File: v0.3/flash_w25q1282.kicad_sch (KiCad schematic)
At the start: 4 parts, among them IC5 W25Q128JVSIM_TR

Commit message: v0.3: lots of routing done
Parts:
- removed NT2: NetTie_2, symbol Device:NetTie_2
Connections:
- net FLASH_3V3 is gone; now on net +3.3V: C39.1, C40.1, IC5.8 (VCC)
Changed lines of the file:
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@@
-	(wire
-		(pts
-			(xy 228.6 105.41) (xy 242.57 105.41)
-		)
-		(stroke
-			(width 0)
-			(type default)
-		)
-	)
 	(wire
 		(pts
@@
 	(wire
 		(pts
-			(xy 212.09 105.41) (xy 223.52 105.41)
+			(xy 212.09 105.41) (xy 242.57 105.41)
 		)
 		(stroke
@@
 					(unit 1)
 				)
-			)
-		)
-	)
-	(symbol
-		(lib_id "Device:NetTie_2")
-		(at 226.06 105.41 0)
-		(unit 1)
-		(exclude_from_sim no)
-		(in_bom no)
-		(on_board yes)
-		(dnp no)
-		(fields_autoplaced yes)
-		(property "Reference" "NT2"
-			(at 226.06 100.33 0)
-			(effects
-				(font
-					(size 1.27 1.27)
-				)
-			)
-		)
-		(property "Value" "NetTie_2"
-			(at 226.06 102.87 0)
-			(effects
-				(font
-					(size 1.27 1.27)
-				)
-			)
-		)
-		(property "Footprint" ""
-			(at 226.06 105.41 0)
-			(effects
-				(font
-					(size 1.27 1.27)
-				)
-				(hide yes)
-			)
-		)
-		(property "Datasheet" "~"
-			(at 226.06 105.41 0)
-			(effects
-				(font
-					(size 1.27 1.27)
-				)
-				(hide yes)
-			)
-		)
-		(property "Description" "Net tie, 2 pins"
-			(at 226.06 105.41 0)
-			(effects
-				(font
-					(size 1.27 1.27)
-				)
-				(hide yes)
-			)
-		)
-		(pin "1"
-		)
-		(pin "2"
-		)
-		(instances
-			(project ""
-				(path "/5cbb45d4-7f83-48dd-a53b-5c75c7d1d827/d61d67cb-51a7-4693-85fc-ed7a034bf235"
-					(reference "NT2")
-					(unit 1)
-				)

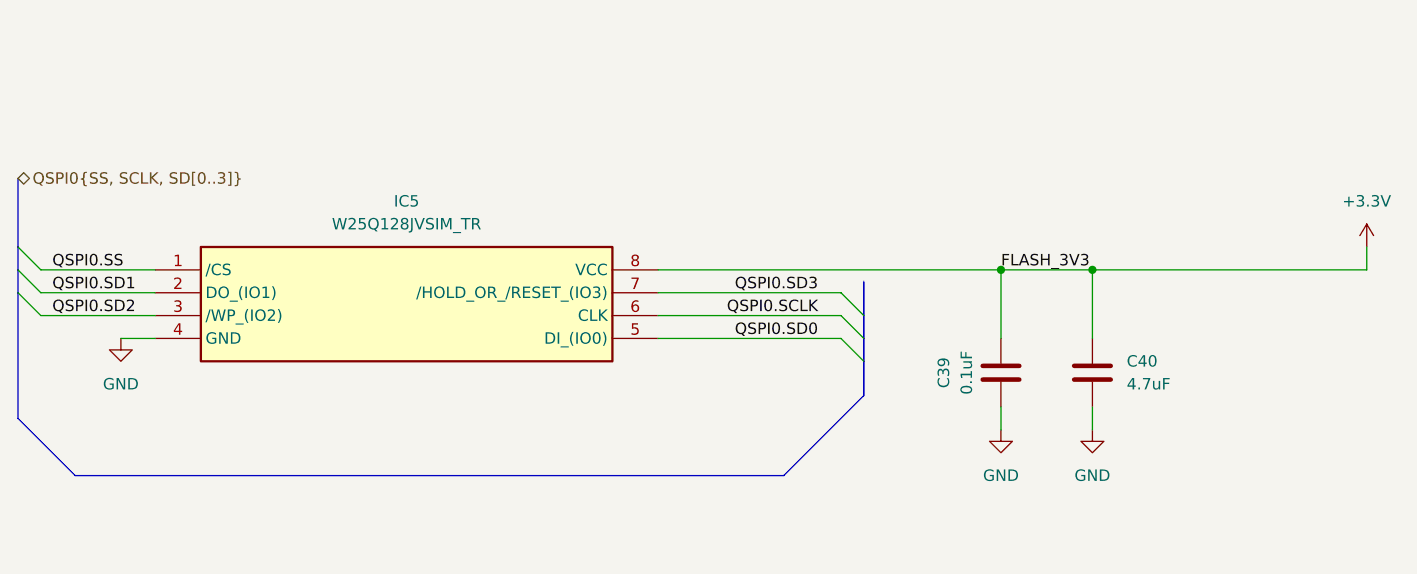
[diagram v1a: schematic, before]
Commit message: v0.3: move pmic to right side of board
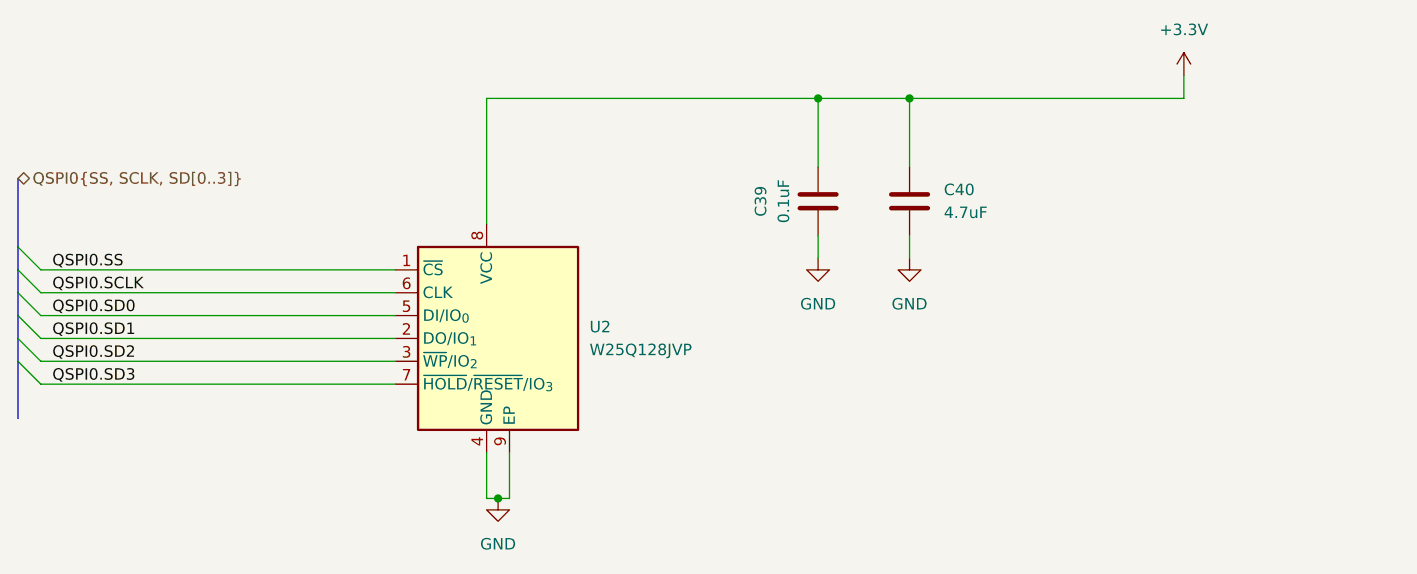
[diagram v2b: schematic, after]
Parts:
- removed IC5: W25Q128JVSIM_TR, SamacSys_Parts:SOIC127P790X216-8N, symbol SamacSys_Parts:W25Q128JVSIM_TR
- added U2: W25Q128JVP, Package_SON:WSON-8-1EP_6x5mm_P1.27mm_EP3.4x4.3mm, symbol Memory_Flash:W25Q128JVP
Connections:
- net +3.3V: now also U2.8 (VCC)
- net GND: now also U2.4 (GND), U2.9 (EP)
- net QSPI0.SCLK: now also U2.6 (CLK)
- net QSPI0.SD0: now also U2.5 (DI/IO_{0})
- net QSPI0.SD1: now also U2.2 (DO/IO_{1})
- net QSPI0.SD2: now also U2.3 (~{WP}/IO_{2})
- net QSPI0.SD3: now also U2.7 (~{HOLD}/~{RESET}/IO_{3})
- net QSPI0.SS: now also U2.1 (~{CS})
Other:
- moved on the sheet: C39, C40
